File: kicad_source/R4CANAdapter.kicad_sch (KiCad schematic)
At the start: 18 parts, among them CN1 CONN_01X05, CN2 691322310004, CN3 GH_SM04B-GHS-TB, CN4 GH_SM04B-GHS-TB, U1 TCAN332GDR

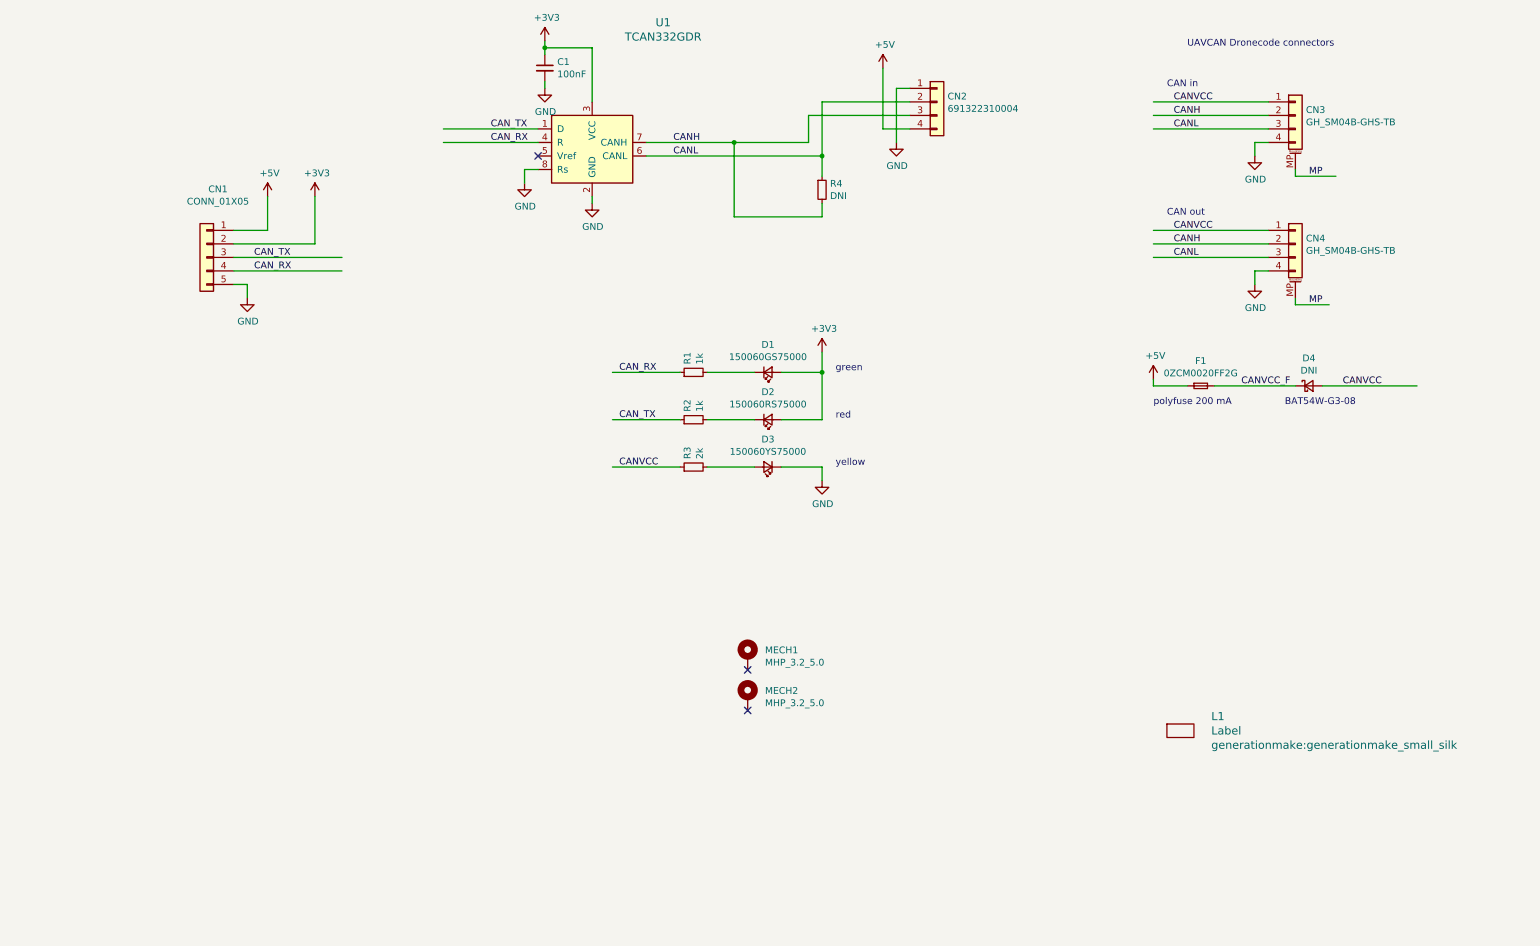
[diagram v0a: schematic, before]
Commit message: added Arduino Uno connector
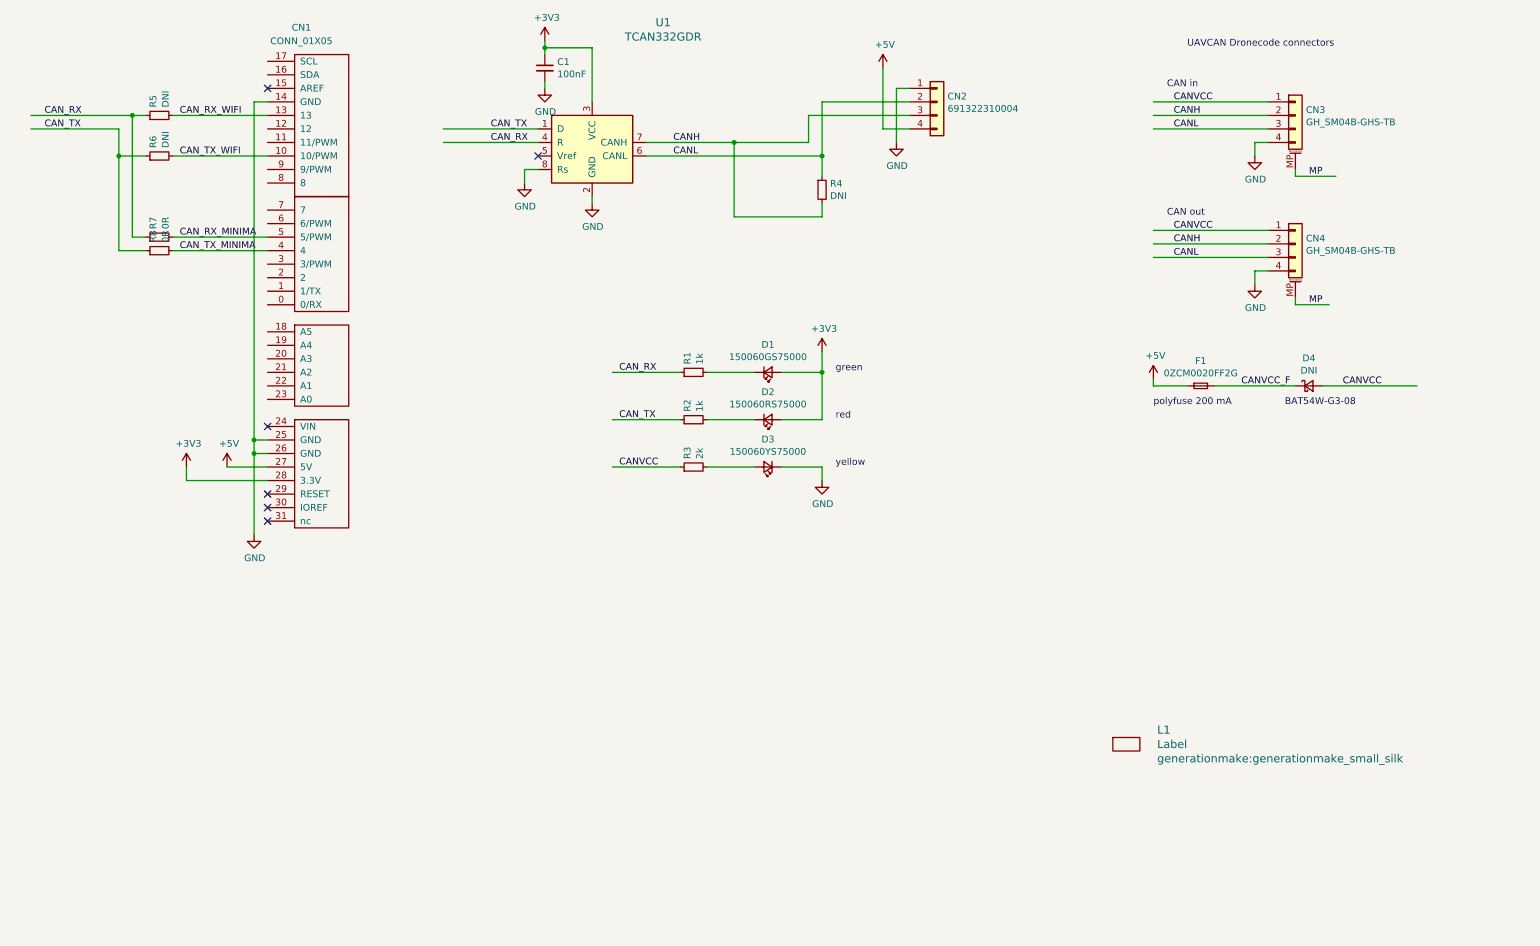
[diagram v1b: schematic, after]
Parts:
- removed MECH1, MECH2: MHP_3.2_5.0, MountingHole:MountingHole_3.2mm_M3, symbol Mechanical:MountingHole_Pad
- added R5, R6: DNI, Resistor_SMD:R_0603_1608Metric, symbol Device:R_Small
- added R7, R8: 0R, Resistor_SMD:R_0603_1608Metric, symbol Device:R_Small
- CN1: footprint Connector_PinHeader_2.54mm:PinHeader_1x05_P2.54mm_Vertical -> generationmake:ARDUINO; symbol Connector_Generic:Conn_01x05 -> generationmake:ARDUINO
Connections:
- net +3V3: now also CN1.28 (3.3V); no longer CN1.2 (Pin_2)
- net +5V: now also CN1.27 (5V); no longer CN1.1 (Pin_1)
- net CAN_RX: now also R5.1, R7.1; no longer CN1.4 (Pin_4)
- net CAN_TX: now also R6.1, R8.1; no longer CN1.3 (Pin_3)
- net GND: now also CN1.14 (GND), CN1.25 (GND), CN1.26 (GND); no longer CN1.5 (Pin_5)
- new net CAN_RX_MINIMA: CN1.5 (5/PWM), R7.2
- new net CAN_RX_WIFI: CN1.13, R5.2
- new net CAN_TX_MINIMA: CN1.4, R8.2
- new net CAN_TX_WIFI: CN1.10 (10/PWM), R6.2
- no-connect marks 3 -> 6
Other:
- moved on the sheet: L1

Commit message: added I2C and eeprom
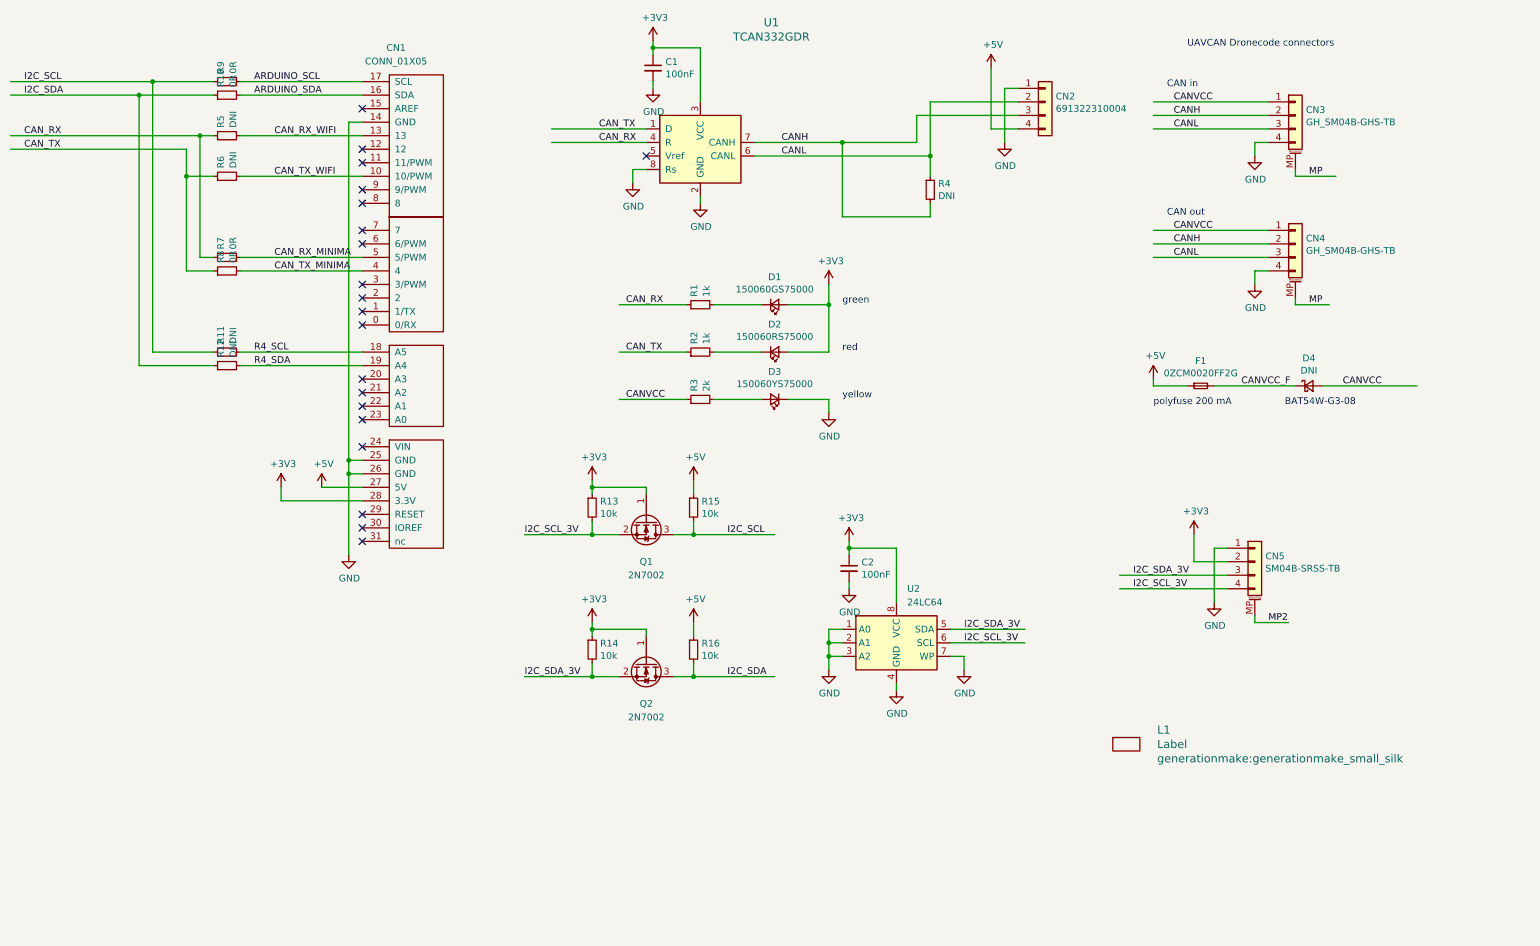
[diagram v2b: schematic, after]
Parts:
- added C2: 100nF, Capacitor_SMD:C_0603_1608Metric, symbol Device:C_Small
- added CN5: SM04B-SRSS-TB, Connector_JST:JST_SH_SM04B-SRSS-TB_1x04-1MP_P1.00mm_Horizontal, symbol Connector_Generic_MountingPin:Conn_01x04_MountingPin
- added Q1, Q2: 2N7002, Package_TO_SOT_SMD:SOT-23, symbol Device:Q_NMOS_GSD
- added R10, R9: 0R, Resistor_SMD:R_0603_1608Metric, symbol Device:R_Small
- added R11, R12: DNI, Resistor_SMD:R_0603_1608Metric, symbol Device:R_Small
- added R13, R14, R15, R16: 10k, Resistor_SMD:R_0603_1608Metric, symbol Device:R_Small
- added U2: 24LC64, Package_SO:SO-8_3.9x4.9mm_P1.27mm, symbol Memory_EEPROM:24LC64
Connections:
- net +3V3: now also C2.1, CN5.2 (Pin_2), Q1.1 (G), Q2.1 (G), R13.1, R14.1, U2.8 (VCC)
- net +5V: now also R15.1, R16.1
- net GND: now also C2.2, CN5.1 (Pin_1), U2.1 (A0), U2.2 (A1), U2.3 (A2), U2.4 (GND), U2.7 (WP)
- net ARDUINO_SDA: now reaches CN1.16 (SDA)
- net ARDUINO_SDA: now also R10.2
- net ARDUINO_SCL: now reaches CN1.17 (SCL)
- net ARDUINO_SCL: now also R9.2
- net R4_SCL: now reaches CN1.18 (A5)
- net R4_SCL: now also R11.2
- net R4_SDA: now reaches CN1.19 (A4)
- net R4_SDA: now also R12.2
- new net I2C_SCL: Q1.3 (D), R11.1, R15.2, R9.1
- new net I2C_SCL_3V: CN5.4 (Pin_4), Q1.2 (S), R13.2, U2.6 (SCL)
- new net I2C_SDA: Q2.3 (D), R10.1, R12.1, R16.2
- new net I2C_SDA_3V: CN5.3 (Pin_3), Q2.2 (S), R14.2, U2.5 (SDA)
- new net MP2: CN5.MP (MountPin)
- no-connect marks 6 -> 20
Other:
- moved on the sheet: C1, CN1, CN2, D1, D2, D3, R1, R2, R3, R4, R5, R6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

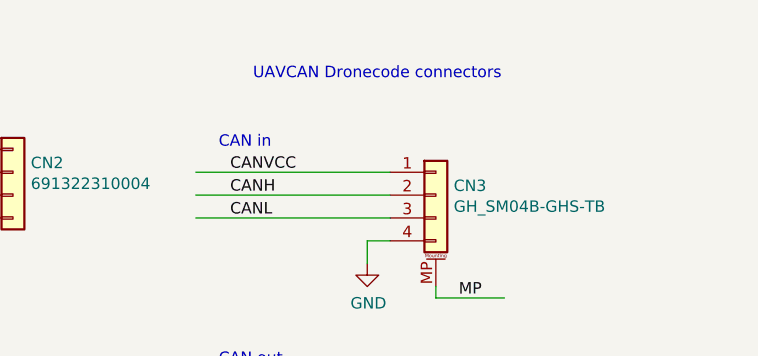
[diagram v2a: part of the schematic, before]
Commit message: added pdf schematic
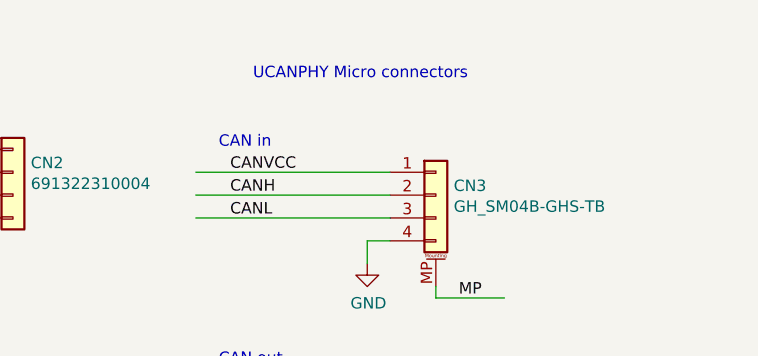
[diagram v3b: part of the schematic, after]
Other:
- note added: "UCANPHY Micro connectors"
- note removed: "UAVCAN Dronecode connectors"
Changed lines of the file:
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@@
   (title_block
     (title "R4CANAdapter")
-    (date "2023-08-13")
+    (date "2023-08-14")
     (rev "0.1")
     (company "generationmake")
@@
     (effects (font (size 1.27 1.27)) (justify left bottom))
   )
-  (text "UAVCAN Dronecode connectors" (at 236.22 22.86 0)
-    (effects (font (size 1.27 1.27)) (justify left bottom))
-  )
+  (text "UCANPHY Micro connectors" (at 236.22 22.86 0)
+    (effects (font (size 1.27 1.27)) (justify left bottom))
+  )

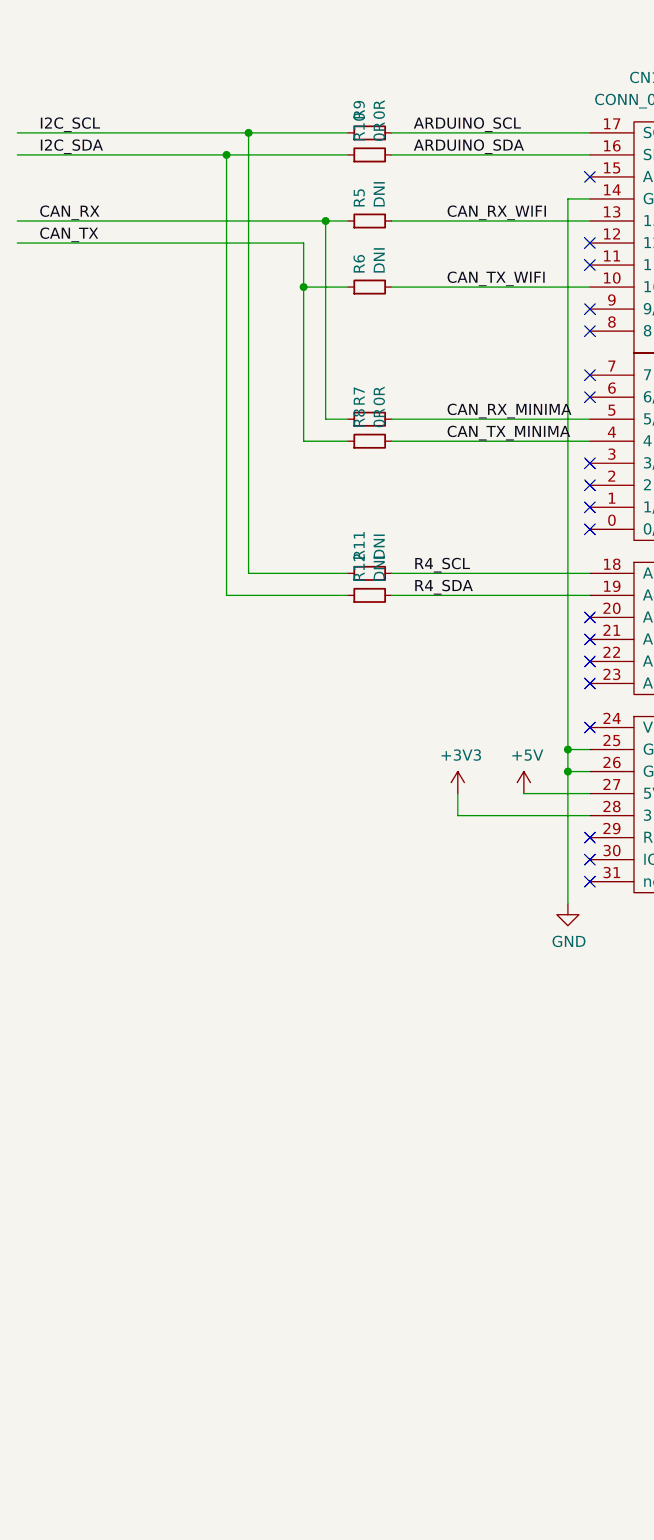
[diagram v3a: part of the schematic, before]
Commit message: used real jumpers
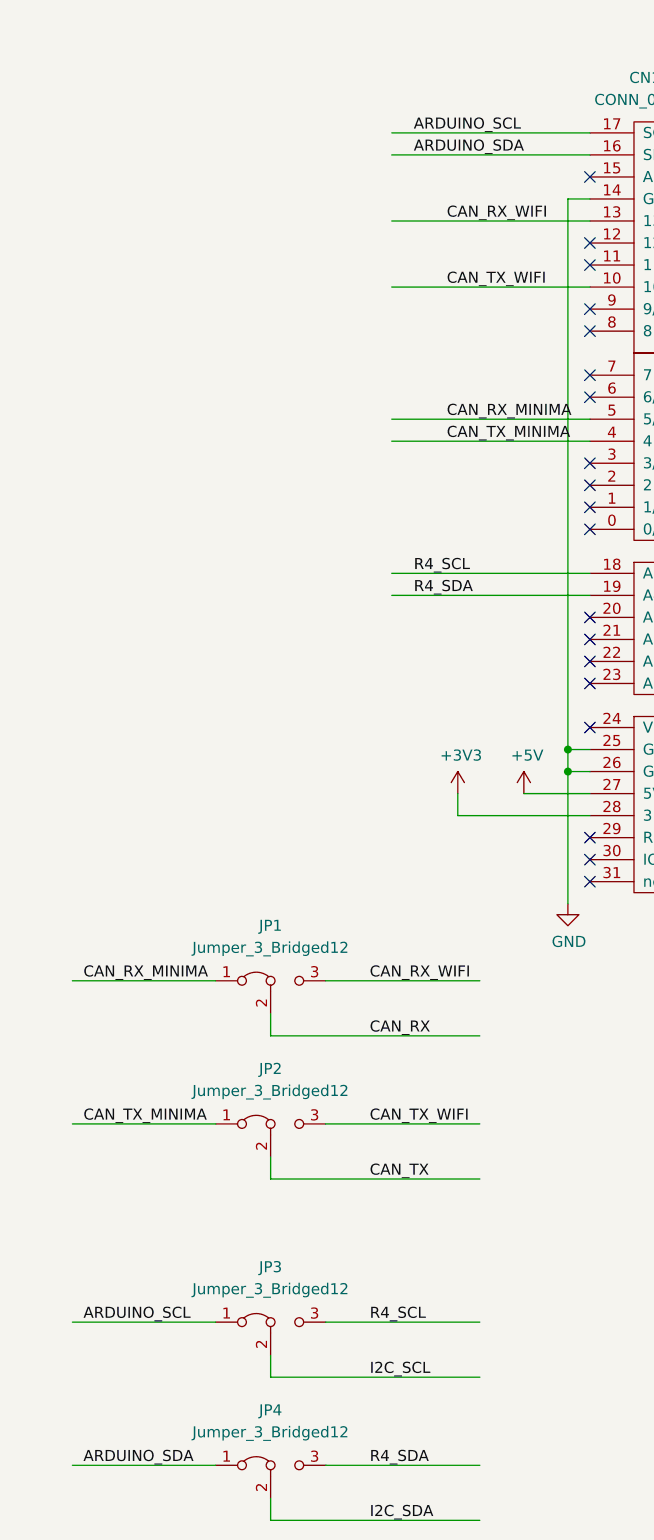
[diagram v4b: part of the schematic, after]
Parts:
- removed R10, R7, R8, R9: 0R, Resistor_SMD:R_0603_1608Metric, symbol Device:R_Small
- removed R11, R12, R5, R6: DNI, Resistor_SMD:R_0603_1608Metric, symbol Device:R_Small
- added JP1, JP2, JP3, JP4: Jumper_3_Bridged12, Connector_PinHeader_2.54mm:PinHeader_1x03_P2.54mm_Vertical, symbol Jumper:Jumper_3_Bridged12
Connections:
- net ARDUINO_SCL: now also JP3.1 (A)
- net ARDUINO_SDA: now also JP4.1 (A)
- net CAN_RX: now also JP1.2 (C)
- net CAN_RX_MINIMA: now also JP1.1 (A)
- net CAN_RX_WIFI: now also JP1.3 (B)
- net CAN_TX: now also JP2.2 (C)
- net CAN_TX_MINIMA: now also JP2.1 (A)
- net CAN_TX_WIFI: now also JP2.3 (B)
- net I2C_SCL: now also JP3.2 (C)
- net I2C_SDA: now also JP4.2 (C)
- net R4_SCL: now also JP3.3 (B)
- net R4_SDA: now also JP4.3 (B)
